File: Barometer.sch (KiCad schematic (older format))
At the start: 5 parts, among them U9 BMP388

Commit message: Lots of changes made
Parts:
- removed U9: BMP388, Footprints:BMP388, symbol JPW_Symbols:BMP388
- added U7: BMP280, Package_LGA:Bosch_LGA-8_2x2.5mm_P0.65mm_ClockwisePinNumbering, symbol Sensor_Pressure:BMP280
- renumbered C9 to C23, C10 to C24, R8 to R10, R5 to R9
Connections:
- net labels added: I2C1_SCL, I2C1_SDA
- net labels removed: I2C3_SCL, I2C3_SDA
- wire segments 16 -> 13
- no-connect marks 1 -> 0
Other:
- note removed: "Barometer"
- moved on the sheet: C23, C24, R10, R9

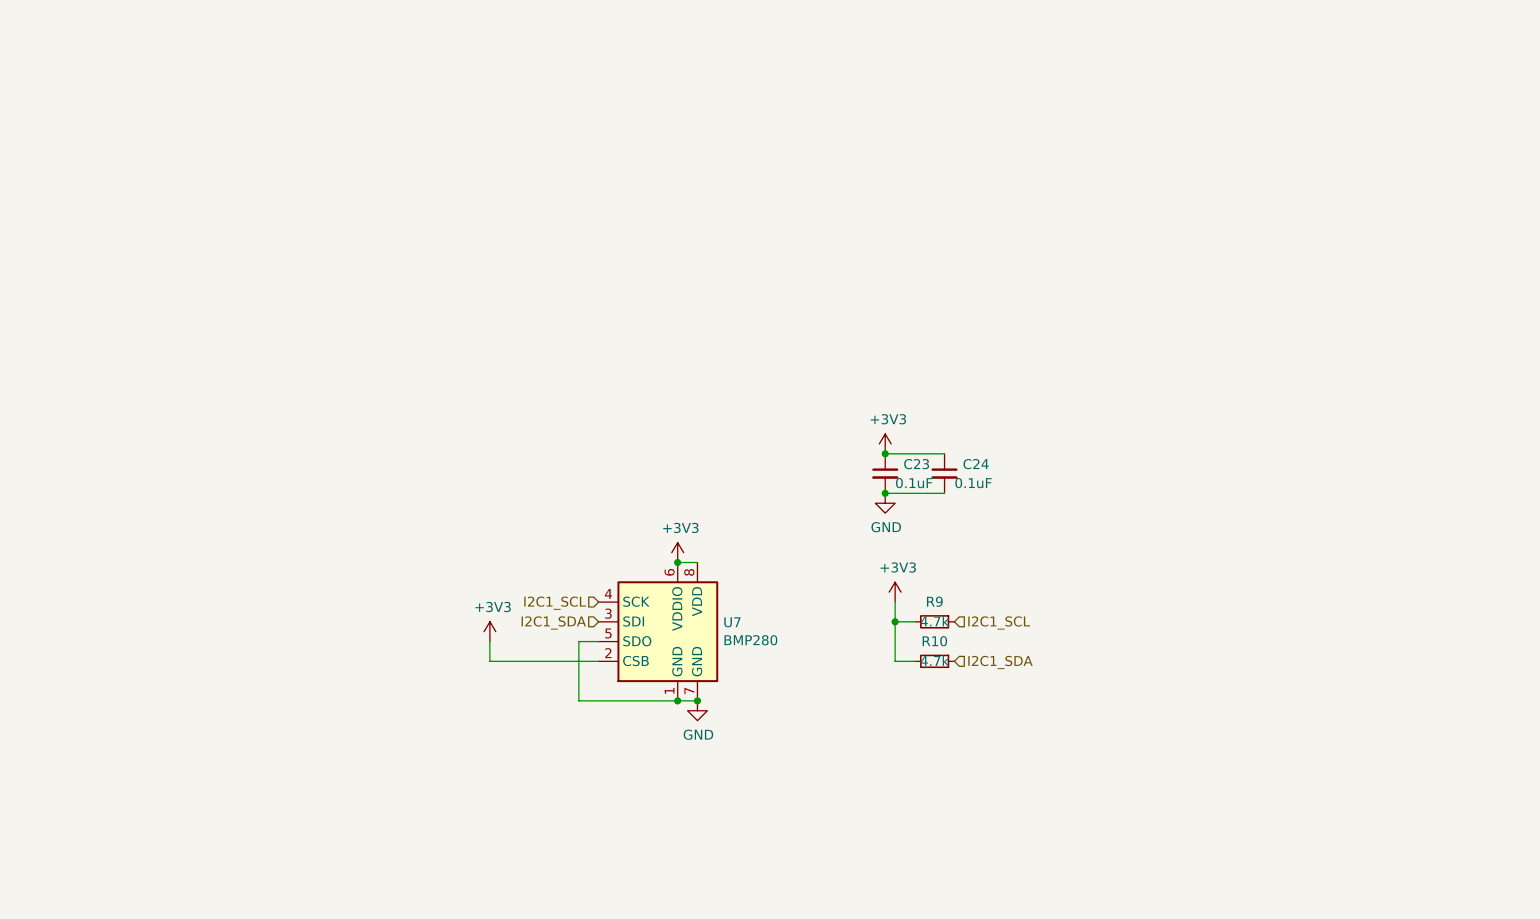
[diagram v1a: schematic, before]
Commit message: Cosmetic changes to schematic
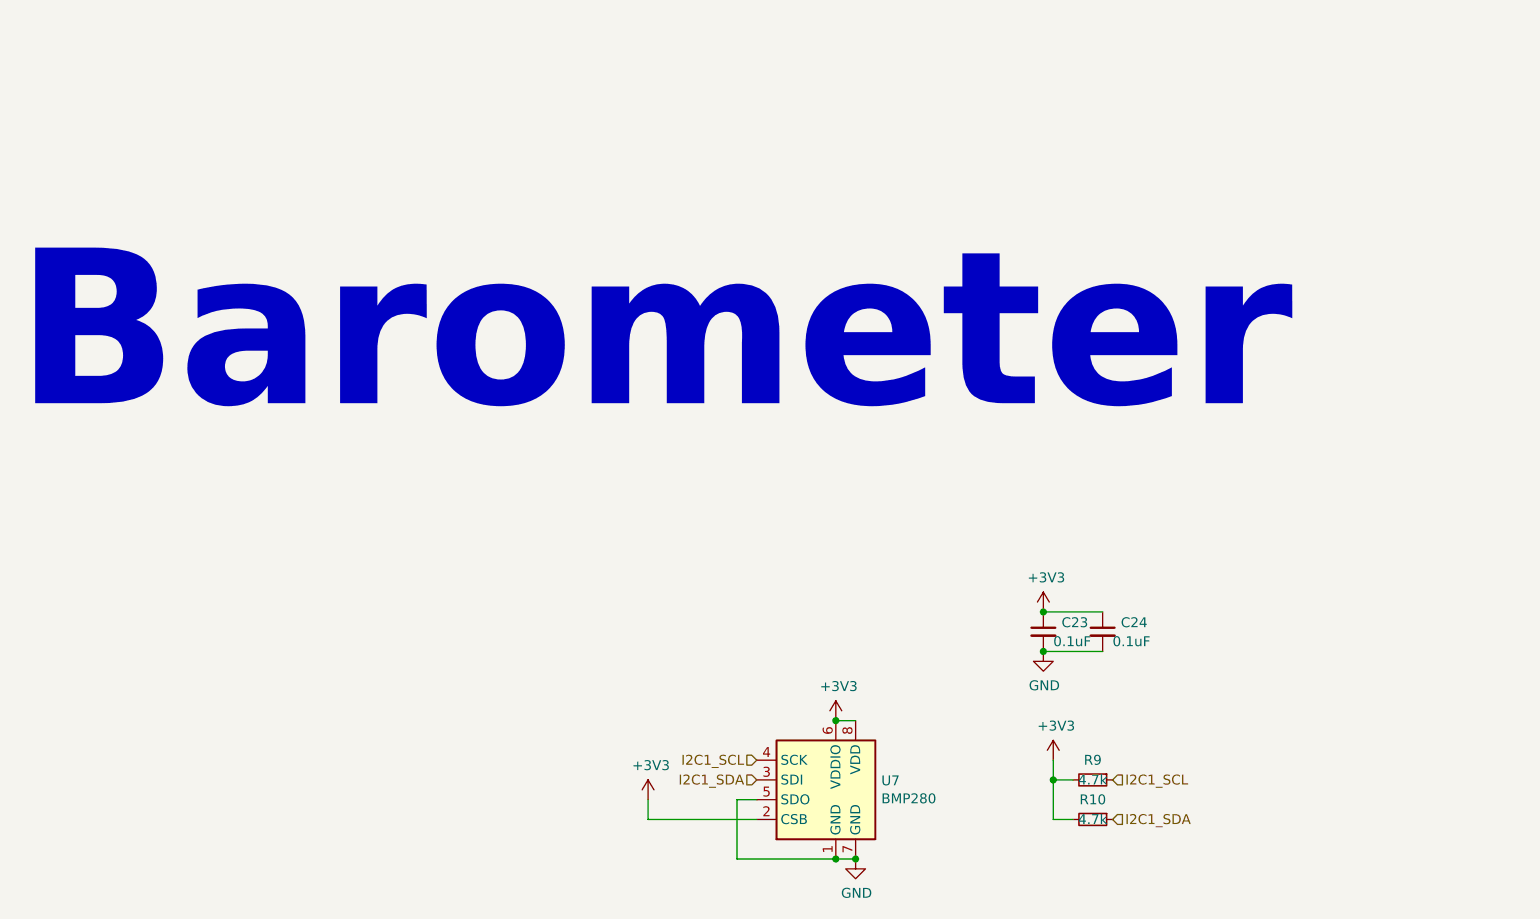
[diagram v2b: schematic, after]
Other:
- note added: "Barometer"
- moved on the sheet: C23, C24, R10, R9, U7

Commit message: Finished routing
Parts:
- R10, R9: value 4.7k -> 2k2
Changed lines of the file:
@@
 P 8150 4650
 F 0 "R9" V 8050 4650 50  0000 C CNN
-F 1 "4.7k" V 8150 4650 50  0000 C CNN
+F 1 "2k2" V 8150 4650 50  0000 C CNN
 F 2 "Resistor_SMD:R_0402_1005Metric" H 8150 4650 50  0001 C CNN
 F 3 "~" H 8150 4650 50  0001 C CNN
@@
 P 8150 4850
 F 0 "R10" V 8050 4850 50  0000 C CNN
-F 1 "4.7k" V 8150 4850 50  0000 C CNN
+F 1 "2k2" V 8150 4850 50  0000 C CNN
 F 2 "Resistor_SMD:R_0402_1005Metric" H 8150 4850 50  0001 C CNN
 F 3 "~" H 8150 4850 50  0001 C CNN

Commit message: Changes made
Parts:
- renumbered C23 to C21, C24 to C22, U7 to U6
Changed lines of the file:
@@
 I2C1_SCL
 $Comp
-L power:+3V3 #PWR043
+L power:+3V3 #PWR037
 U 1 1 608E9117
 P 6850 4350
-F 0 "#PWR043" H 6850 4200 50  0001 C CNN
+F 0 "#PWR037" H 6850 4200 50  0001 C CNN
 F 1 "+3V3" H 6865 4523 50  0000 C CNN
 F 2 "" H 6850 4350 50  0001 C CNN
@@
 $EndComp
 $Comp
-L power:GND #PWR046
+L power:GND #PWR040
 U 1 1 608EAE19
 P 6950 5050
-F 0 "#PWR046" H 6950 4800 50  0001 C CNN
+F 0 "#PWR040" H 6950 4800 50  0001 C CNN
 F 1 "GND" H 6955 4877 50  0000 C CNN
 F 2 "" H 6950 5050 50  0001 C CNN
@@
 	6950 5050 6850 5050
 $Comp
-L power:+3V3 #PWR044
+L power:+3V3 #PWR038
 U 1 1 60872AF9
 P 7950 4550
-F 0 "#PWR044" H 7950 4400 50  0001 C CNN
+F 0 "#PWR038" H 7950 4400 50  0001 C CNN
 F 1 "+3V3" H 7965 4723 50  0000 C CNN
 F 2 "" H 7950 4550 50  0001 C CNN
@@
 Connection ~ 7950 4650
 $Comp
-L power:+3V3 #PWR041
+L power:+3V3 #PWR035
 U 1 1 60875CC0
 P 7900 3800
-F 0 "#PWR041" H 7900 3650 50  0001 C CNN
+F 0 "#PWR035" H 7900 3650 50  0001 C CNN
 F 1 "+3V3" H 7915 3973 50  0000 C CNN
 F 2 "" H 7900 3800 50  0001 C CNN
@@
 $EndComp
 $Comp
-L Device:C_Small C24
+L Device:C_Small C22
 U 1 1 60876227
 P 8200 3900
-F 0 "C24" H 8292 3946 50  0000 L CNN
+F 0 "C22" H 8292 3946 50  0000 L CNN
 F 1 "0.1uF" H 8250 3850 50  0000 L CNN
 F 2 "Capacitor_SMD:C_0402_1005Metric" H 8200 3900 50  0001 C CNN
@@
 $EndComp
 $Comp
-L Device:C_Small C23
+L Device:C_Small C21
 U 1 1 6087626C
 P 7900 3900
-F 0 "C23" H 7992 3946 50  0000 L CNN
+F 0 "C21" H 7992 3946 50  0000 L CNN
 F 1 "0.1uF" H 7950 3850 50  0000 L CNN
 F 2 "Capacitor_SMD:C_0402_1005Metric" H 7900 3900 50  0001 C CNN
@@
 	7900 3800 8200 3800
 $Comp
-L power:GND #PWR042
+L power:GND #PWR036
 U 1 1 60877E25
 P 7900 4000
-F 0 "#PWR042" H 7900 3750 50  0001 C CNN
+F 0 "#PWR036" H 7900 3750 50  0001 C CNN
 F 1 "GND" H 7905 3827 50  0000 C CNN
 F 2 "" H 7900 4000 50  0001 C CNN
@@
 	7900 4000 8200 4000
 $Comp
-L Sensor_Pressure:BMP280 U7
+L Sensor_Pressure:BMP280 U6
 U 1 1 60D6237A
 P 6850 4750
-F 0 "U7" H 7080 4846 50  0000 L CNN
+F 0 "U6" H 7080 4846 50  0000 L CNN
 F 1 "BMP280" H 7080 4755 50  0000 L CNN
 F 2 "Package_LGA:Bosch_LGA-8_2x2.5mm_P0.65mm_ClockwisePinNumbering" H 6850 4050 50  0001 C CNN
@@
 Connection ~ 6850 5050
 $Comp
-L power:+3V3 #PWR045
+L power:+3V3 #PWR039
 U 1 1 60D6B9F1
 P 5900 4750
-F 0 "#PWR045" H 5900 4600 50  0001 C CNN
+F 0 "#PWR039" H 5900 4600 50  0001 C CNN
 F 1 "+3V3" H 5915 4923 50  0000 C CNN
 F 2 "" H 5900 4750 50  0001 C CNN
